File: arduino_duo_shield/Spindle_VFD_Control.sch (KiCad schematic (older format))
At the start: 14 parts, among them P18 CONN_01X01, P19 CONN_01X01, P20 CONN_01X01, P21 CONN_01X01, Q3 2N7000, Q4 BS250, U7 PC817

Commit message: Recalculate paths of spindle adapter
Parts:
- removed R22: 10k, symbol Device:RTRIM
- added D3, D4: 1N4007, Diode_THT:D_A-405_P7.62mm_Horizontal, symbol Device:D_ALT
- added D5: 1N4007, symbol Device:D_ALT
- added K2, K3: JQC-3F, Relay_THT:Relay_SPDT_SANYOU_SRD_Series_Form_C, symbol Relay:G5LE-1
- added Q5, Q6: 2N7000, Package_TO_SOT_THT:TO-92_Inline, symbol Transistor_FET:2N7000
- added R22: 220, Resistor_THT:R_Axial_DIN0204_L3.6mm_D1.6mm_P5.08mm_Horizontal, symbol Device:R
- added R25, R26: 10K, Resistor_THT:R_Axial_DIN0204_L3.6mm_D1.6mm_P5.08mm_Horizontal, symbol Device:R
- added RV1: 100K, symbol Device:R_POT_TRIM
- added U8, U9: PC817, Package_DIP:DIP-4_W7.62mm, symbol Isolator:PC817
- R24: value 56k -> 220
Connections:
- net labels added: ext_spdir, ext_spenab, ext_vcc, inverter_12V, inverter_bw_switch, inverter_frequency_10V, inverter_fw_switch, inverter_gnd
- net labels removed: ext_vdd, motor_ctl_sprot
- wire segments 34 -> 73
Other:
- moved on the sheet: C8, L1, Q3, Q4, R15, R21, R23, U7

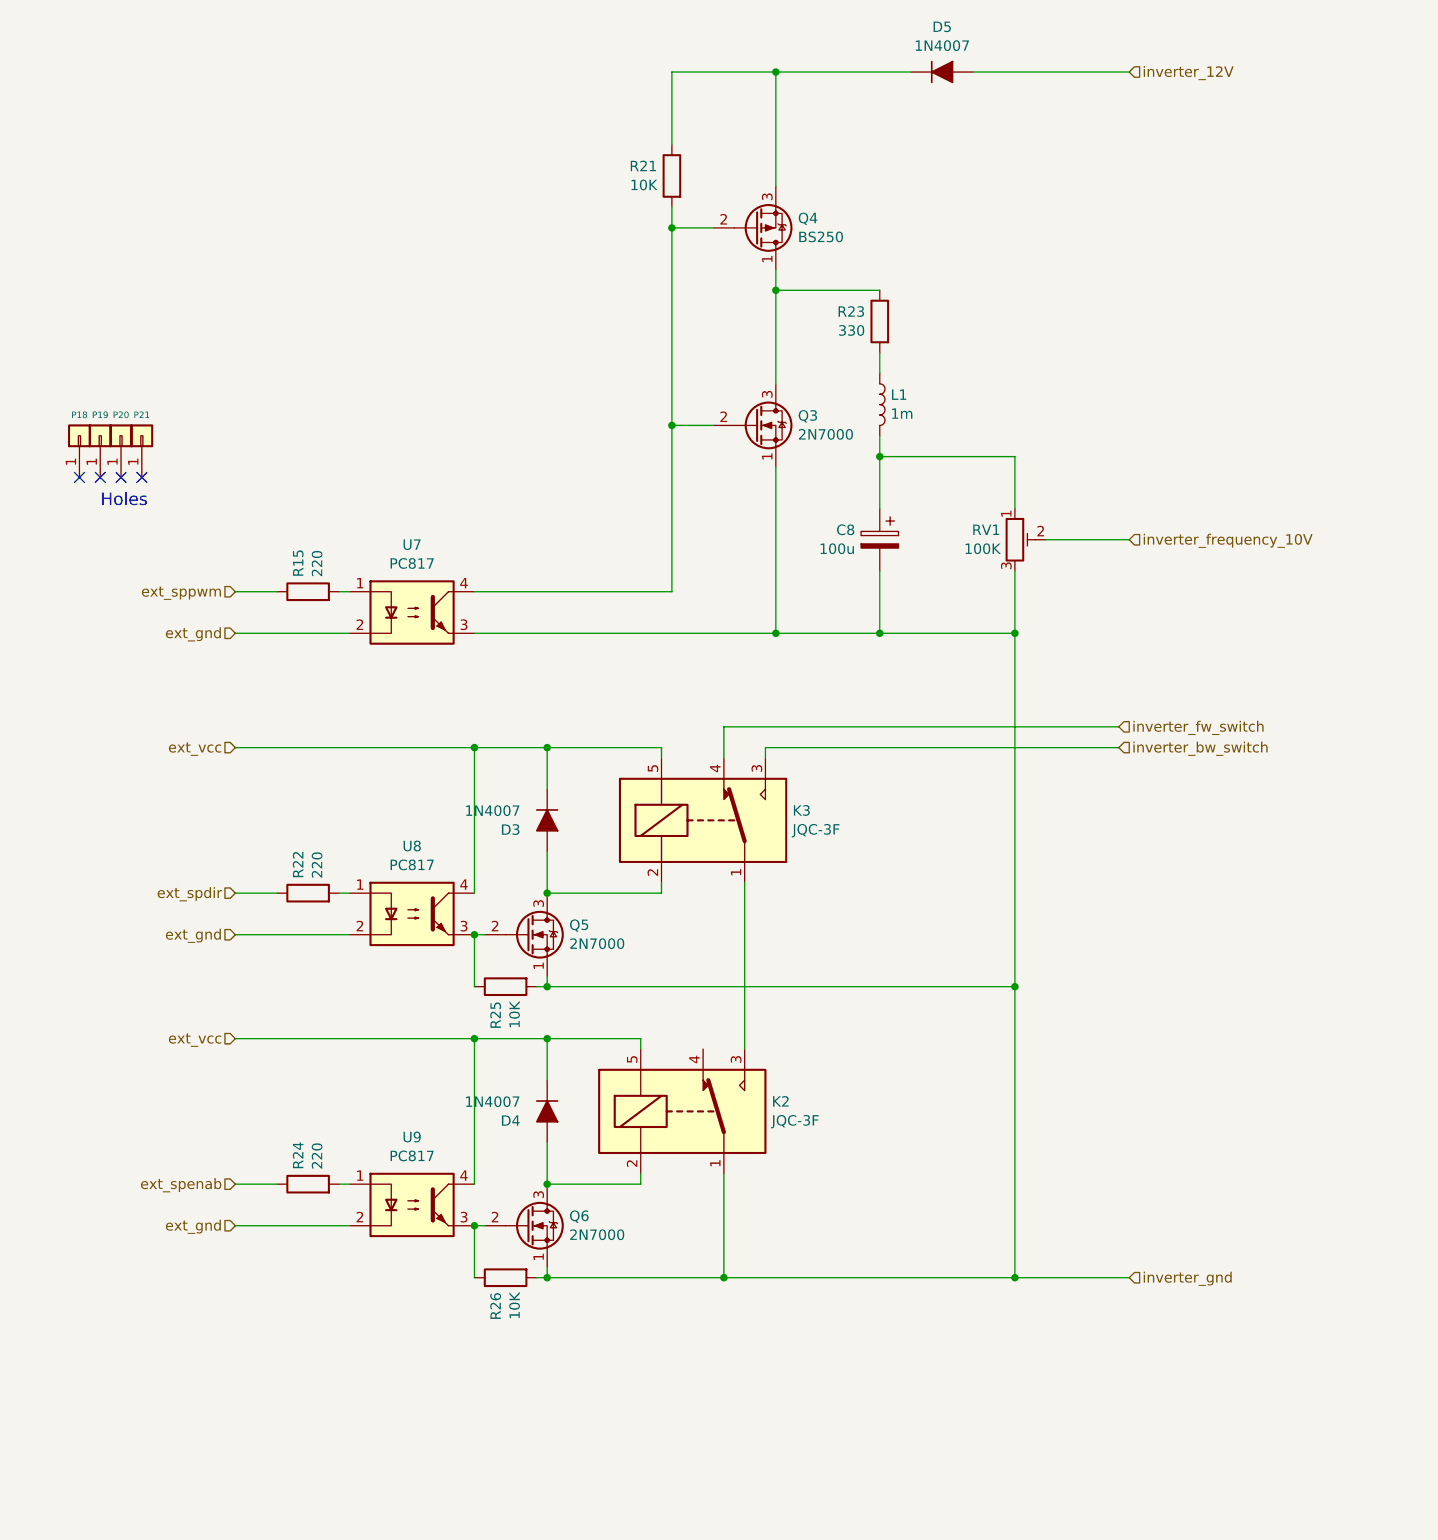
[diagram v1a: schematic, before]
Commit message: Add signal mirror and control jumpers
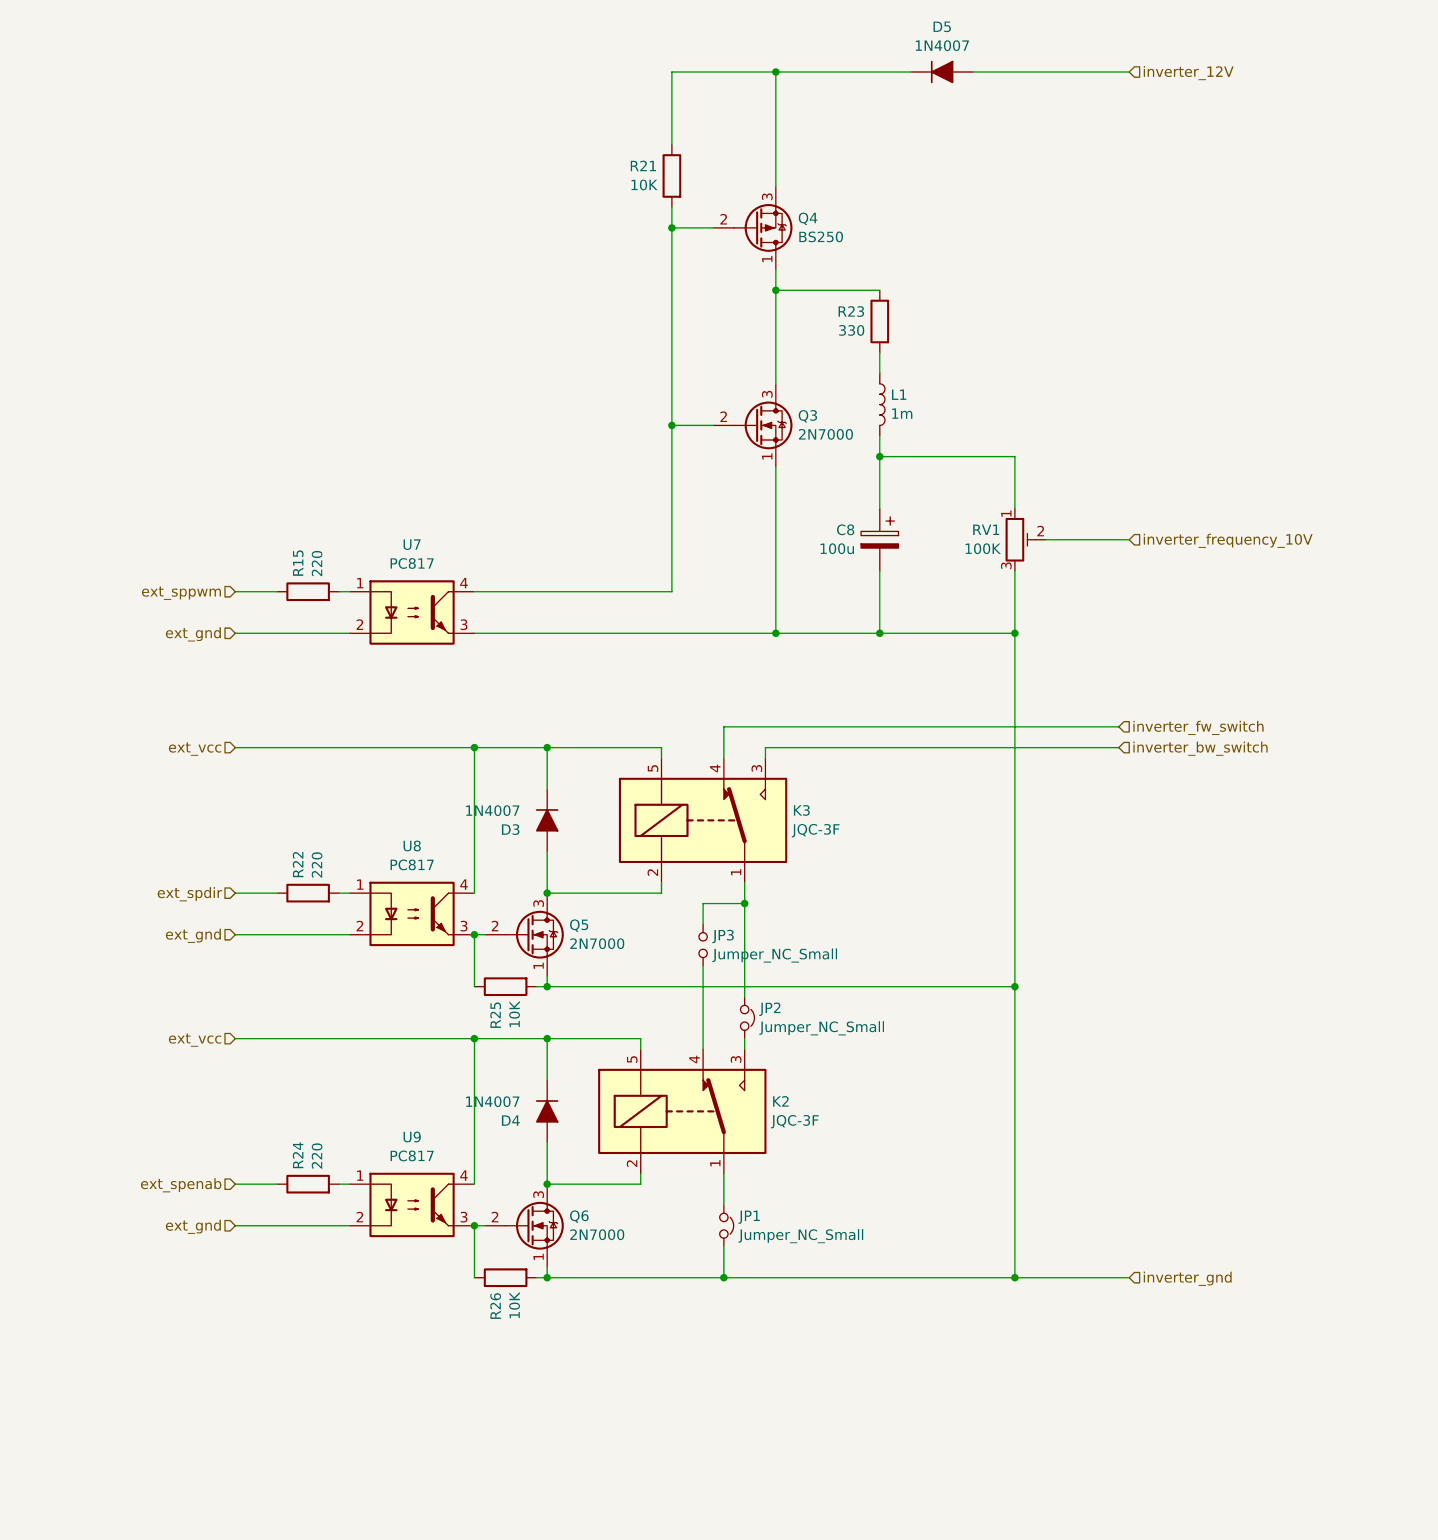
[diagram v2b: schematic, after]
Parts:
- removed P18, P19, P20, P21: CONN_01X01, Socket_Arduino_Mega:Arduino_1pin, symbol Connector_Generic:Conn_01x01
- added JP1, JP2: Jumper_NC_Small, Connector_PinHeader_2.54mm:PinHeader_1x02_P2.54mm_Vertical, symbol Device:Jumper_NC_Small
- added JP3: Jumper_NC_Small, Connector_PinHeader_2.54mm:PinHeader_1x02_P2.54mm_Vertical, symbol Device:Jumper_NO_Small
- C8: footprint (none) -> Capacitor_THT:C_Disc_D3.0mm_W2.0mm_P2.50mm
- D5: footprint (none) -> Diode_THT:D_A-405_P7.62mm_Horizontal
- L1: footprint (none) -> Inductor_THT:L_Axial_L7.0mm_D3.3mm_P10.16mm_Horizontal_Fastron_MICC
- R15, R21, R22, R24, R25, R26: footprint Resistor_THT:R_Axial_DIN0204_L3.6mm_D1.6mm_P5.08mm_Horizontal -> Resistor_THT:R_Axial_DIN0207_L6.3mm_D2.5mm_P7.62mm_Horizontal
- R23: footprint Resistor_THT:R_Axial_DIN0204_L3.6mm_D1.6mm_P5.08mm_Horizontal -> Resistor_THT:R_Axial_DIN0309_L9.0mm_D3.2mm_P12.70mm_Horizontal
- RV1: footprint (none) -> Potentiometer_THT:Potentiometer_Bourns_3296W_Vertical
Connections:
- net inverter_gnd: now also JP1.2; no longer K2.1
- net at K3.1: now also JP2.1, JP3.1; no longer K2.3
- net at K2.4: now also JP3.2
- new net: JP1.1, K2.1
- new net: JP2.2, K2.3
- no-connect marks 4 -> 0
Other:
- note removed: "Holes"
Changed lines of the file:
@@
 EESchema Schematic File Version 4
-LIBS:arduino_duo_shield-cache
 EELAYER 30 0
 EELAYER END
@@
 Comment4 ""
 $EndDescr
-Text Notes 1300 2900 0    60   ~ 0
-Holes
-$Comp
-L Connector_Generic:Conn_01x01 P?
-U 1 1 5DD5BB6B
-P 1200 2550
-AR Path="/5DD5BB6B" Ref="P?"  Part="1"
-AR Path="/5D7DFDC0/5DD5BB6B" Ref="P?"  Part="1"
-AR Path="/5DD17641/5DD5BB6B" Ref="P18"  Part="1"
-F 0 "P18" V 1300 2550 31  0000 C CNN
-F 1 "CONN_01X01" V 1300 2550 50  0001 C CNN
-F 2 "Socket_Arduino_Mega:Arduino_1pin" H 1200 2550 50  0001 C CNN
-F 3 "" H 1200 2550 50  0000 C CNN
-	1    1200 2550
-	0    -1   -1   0
-$EndComp
-$Comp
-L Connector_Generic:Conn_01x01 P?
-U 1 1 5DD5BB71
-P 1300 2550
-AR Path="/5DD5BB71" Ref="P?"  Part="1"
-AR Path="/5D7DFDC0/5DD5BB71" Ref="P?"  Part="1"
-AR Path="/5DD17641/5DD5BB71" Ref="P19"  Part="1"
-F 0 "P19" V 1400 2550 31  0000 C CNN
-F 1 "CONN_01X01" V 1400 2550 50  0001 C CNN
-F 2 "Socket_Arduino_Mega:Arduino_1pin" H 1300 2550 50  0001 C CNN
-F 3 "" H 1300 2550 50  0000 C CNN
-	1    1300 2550
-	0    -1   -1   0
-$EndComp
-$Comp
-L Connector_Generic:Conn_01x01 P?
-U 1 1 5DD5BB77
-P 1400 2550
-AR Path="/5DD5BB77" Ref="P?"  Part="1"
-AR Path="/5D7DFDC0/5DD5BB77" Ref="P?"  Part="1"
-AR Path="/5DD17641/5DD5BB77" Ref="P20"  Part="1"
-F 0 "P20" V 1500 2550 31  0000 C CNN
-F 1 "CONN_01X01" V 1500 2550 50  0001 C CNN
-F 2 "Socket_Arduino_Mega:Arduino_1pin" H 1400 2550 50  0001 C CNN
-F 3 "" H 1400 2550 50  0000 C CNN
-	1    1400 2550
-	0    -1   -1   0
-$EndComp
-$Comp
-L Connector_Generic:Conn_01x01 P?
-U 1 1 5DD5BB7D
-P 1500 2550
-AR Path="/5DD5BB7D" Ref="P?"  Part="1"
-AR Path="/5D7DFDC0/5DD5BB7D" Ref="P?"  Part="1"
-AR Path="/5DD17641/5DD5BB7D" Ref="P21"  Part="1"
-F 0 "P21" V 1600 2550 31  0000 C CNN
-F 1 "CONN_01X01" V 1600 2550 50  0001 C CNN
-F 2 "Socket_Arduino_Mega:Arduino_1pin" H 1500 2550 50  0001 C CNN
-F 3 "" H 1500 2550 50  0000 C CNN
-	1    1500 2550
-	0    -1   -1   0
-$EndComp
-NoConn ~ 1200 2750
-NoConn ~ 1300 2750
-NoConn ~ 1400 2750
-NoConn ~ 1500 2750
 Text HLabel 6250 800  2    50   Input ~ 0
 inverter_12V
@@
 F 0 "R23" H 5120 2046 50  0000 L CNN
 F 1 "330" H 5120 1955 50  0000 L CNN
-F 2 "Resistor_THT:R_Axial_DIN0204_L3.6mm_D1.6mm_P5.08mm_Horizontal" V 4980 2000 50  0001 C CNN
+F 2 "Resistor_THT:R_Axial_DIN0309_L9.0mm_D3.2mm_P12.70mm_Horizontal" V 4980 2000 50  0001 C CNN
 F 3 "~" H 5050 2000 50  0001 C CNN
 	1    5050 2000
@@
 F 0 "L1" H 5102 2446 50  0000 L CNN
 F 1 "1m" H 5102 2355 50  0000 L CNN
-F 2 "" H 5050 2400 50  0001 C CNN
+F 2 "Inductor_THT:L_Axial_L7.0mm_D3.3mm_P10.16mm_Horizontal_Fastron_MICC" H 5050 2400 50  0001 C CNN
 F 3 "~" H 5050 2400 50  0001 C CNN
 	1    5050 2400
@@
 F 0 "C8" H 5168 3096 50  0000 L CNN
 F 1 "100u" H 5168 3005 50  0000 L CNN
-F 2 "" H 5088 2900 50  0001 C CNN
+F 2 "Capacitor_THT:C_Disc_D3.0mm_W2.0mm_P2.50mm" H 5088 2900 50  0001 C CNN
 F 3 "~" H 5050 3050 50  0001 C CNN
 	1    5050 3050
@@
 F 0 "R21" H 4120 1346 50  0000 L CNN
 F 1 "10K" H 4120 1255 50  0000 L CNN
-F 2 "Resistor_THT:R_Axial_DIN0204_L3.6mm_D1.6mm_P5.08mm_Horizontal" V 3980 1300 50  0001 C CNN
+F 2 "Resistor_THT:R_Axial_DIN0207_L6.3mm_D2.5mm_P7.62mm_Horizontal" V 3980 1300 50  0001 C CNN
 F 3 "~" H 4050 1300 50  0001 C CNN
 	1    4050 1300
@@
 F 0 "R15" H 2370 3346 50  0000 L CNN
 F 1 "220" H 2370 3255 50  0000 L CNN
-F 2 "Resistor_THT:R_Axial_DIN0204_L3.6mm_D1.6mm_P5.08mm_Horizontal" V 2230 3300 50  0001 C CNN
+F 2 "Resistor_THT:R_Axial_DIN0207_L6.3mm_D2.5mm_P7.62mm_Horizontal" V 2230 3300 50  0001 C CNN
 F 3 "~" H 2300 3300 50  0001 C CNN
 	1    2300 3300
@@
 F 0 "RV1" H 5631 3096 50  0000 R CNN
 F 1 "100K" H 5631 3005 50  0000 R CNN
-F 2 "" H 5700 3050 50  0001 C CNN
+F 2 "Potentiometer_THT:Potentiometer_Bourns_3296W_Vertical" H 5700 3050 50  0001 C CNN
 F 3 "~" H 5700 3050 50  0001 C CNN
 	1    5700 3050
@@
 F 0 "D5" H 5350 1016 50  0000 C CNN
 F 1 "1N4007" H 5350 925 50  0000 C CNN
-F 2 "" H 5350 800 50  0001 C CNN
+F 2 "Diode_THT:D_A-405_P7.62mm_Horizontal" H 5350 800 50  0001 C CNN
 F 3 "~" H 5350 800 50  0001 C CNN
 	1    5350 800
@@
 F 0 "R22" H 2370 4796 50  0000 L CNN
 F 1 "220" H 2370 4705 50  0000 L CNN
-F 2 "Resistor_THT:R_Axial_DIN0204_L3.6mm_D1.6mm_P5.08mm_Horizontal" V 2230 4750 50  0001 C CNN
+F 2 "Resistor_THT:R_Axial_DIN0207_L6.3mm_D2.5mm_P7.62mm_Horizontal" V 2230 4750 50  0001 C CNN
 F 3 "~" H 2300 4750 50  0001 C CNN
 	1    2300 4750
@@
 F 0 "R25" H 3320 5246 50  0000 L CNN
 F 1 "10K" H 3320 5155 50  0000 L CNN
-F 2 "Resistor_THT:R_Axial_DIN0204_L3.6mm_D1.6mm_P5.08mm_Horizontal" V 3180 5200 50  0001 C CNN
+F 2 "Resistor_THT:R_Axial_DIN0207_L6.3mm_D2.5mm_P7.62mm_Horizontal" V 3180 5200 50  0001 C CNN
 F 3 "~" H 3250 5200 50  0001 C CNN
 	1    3250 5200
@@
 F 0 "R24" H 2370 6196 50  0000 L CNN
 F 1 "220" H 2370 6105 50  0000 L CNN
-F 2 "Resistor_THT:R_Axial_DIN0204_L3.6mm_D1.6mm_P5.08mm_Horizontal" V 2230 6150 50  0001 C CNN
+F 2 "Resistor_THT:R_Axial_DIN0207_L6.3mm_D2.5mm_P7.62mm_Horizontal" V 2230 6150 50  0001 C CNN
 F 3 "~" H 2300 6150 50  0001 C CNN
 	1    2300 6150
@@
 F 0 "R26" H 3320 6646 50  0000 L CNN
 F 1 "10K" H 3320 6555 50  0000 L CNN
-F 2 "Resistor_THT:R_Axial_DIN0204_L3.6mm_D1.6mm_P5.08mm_Horizontal" V 3180 6600 50  0001 C CNN
+F 2 "Resistor_THT:R_Axial_DIN0207_L6.3mm_D2.5mm_P7.62mm_Horizontal" V 3180 6600 50  0001 C CNN
 F 3 "~" H 3250 6600 50  0001 C CNN
 	1    3250 6600
@@
 Connection ~ 4050 2500
 Wire Wire Line
-	4300 6100 4300 6600
+	4300 6100 4300 6250
 Wire Wire Line
 	4300 6600 3450 6600
@@
 	4300 6600 5700 6600
 Connection ~ 4300 6600
-Wire Wire Line
-	3450 5200 5700 5200
 Wire Wire Line
 	5700 5200 5700 6600
@@
 	5700 6600 6250 6600
 Wire Wire Line
-	4400 4700 4400 5500
-Wire Wire Line
 	3450 5450 3450 5650
 Wire Wire Line
@@
 Connection ~ 5700 3500
 Connection ~ 5700 5200
+Wire Wire Line
+	4400 4700 4400 4800
+$Comp
+L Device:Jumper_NC_Small JP2
+U 1 1 5E3ED52D
+P 4400 5350
+F 0 "JP2" V 4354 5424 50  0000 L CNN
+F 1 "Jumper_NC_Small" V 4445 5424 50  0000 L CNN
+F 2 "Connector_PinHeader_2.54mm:PinHeader_1x02_P2.54mm_Vertical" H 4400 5350 50  0001 C CNN
+F 3 "~" H 4400 5350 50  0001 C CNN
+	1    4400 5350
+	0    1    1    0
+$EndComp
+Wire Wire Line
+	4400 5450 4400 5500
+$Comp
+L Device:Jumper_NC_Small JP1
+U 1 1 5E3EDC9D
+P 4300 6350
+F 0 "JP1" V 4254 6424 50  0000 L CNN
+F 1 "Jumper_NC_Small" V 4345 6424 50  0000 L CNN
+F 2 "Connector_PinHeader_2.54mm:PinHeader_1x02_P2.54mm_Vertical" H 4300 6350 50  0001 C CNN
+F 3 "~" H 4300 6350 50  0001 C CNN
+	1    4300 6350
+	0    1    1    0
+$EndComp
+Wire Wire Line
+	4300 6450 4300 6600
+Wire Wire Line
+	4200 4800 4400 4800
+Connection ~ 4400 4800
+Wire Wire Line
+	4400 4800 4400 5250
+Wire Wire Line
+	3450 5200 5700 5200
+Wire Wire Line
+	4200 5500 4200 5100
+Wire Wire Line
+	4200 4900 4200 4800
+$Comp
+L Device:Jumper_NO_Small JP3
+U 1 1 5E5C3601
+P 4200 5000
+F 0 "JP3" V 4154 5048 50  0000 L CNN
+F 1 "Jumper_NC_Small" V 4245 5048 50  0000 L CNN
+F 2 "Connector_PinHeader_2.54mm:PinHeader_1x02_P2.54mm_Vertical" H 4200 5000 50  0001 C CNN
+F 3 "~" H 4200 5000 50  0001 C CNN
+	1    4200 5000
+	0    1    1    0
+$EndComp
 $EndSCHEMATC
